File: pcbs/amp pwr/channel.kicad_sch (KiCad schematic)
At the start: 43 parts

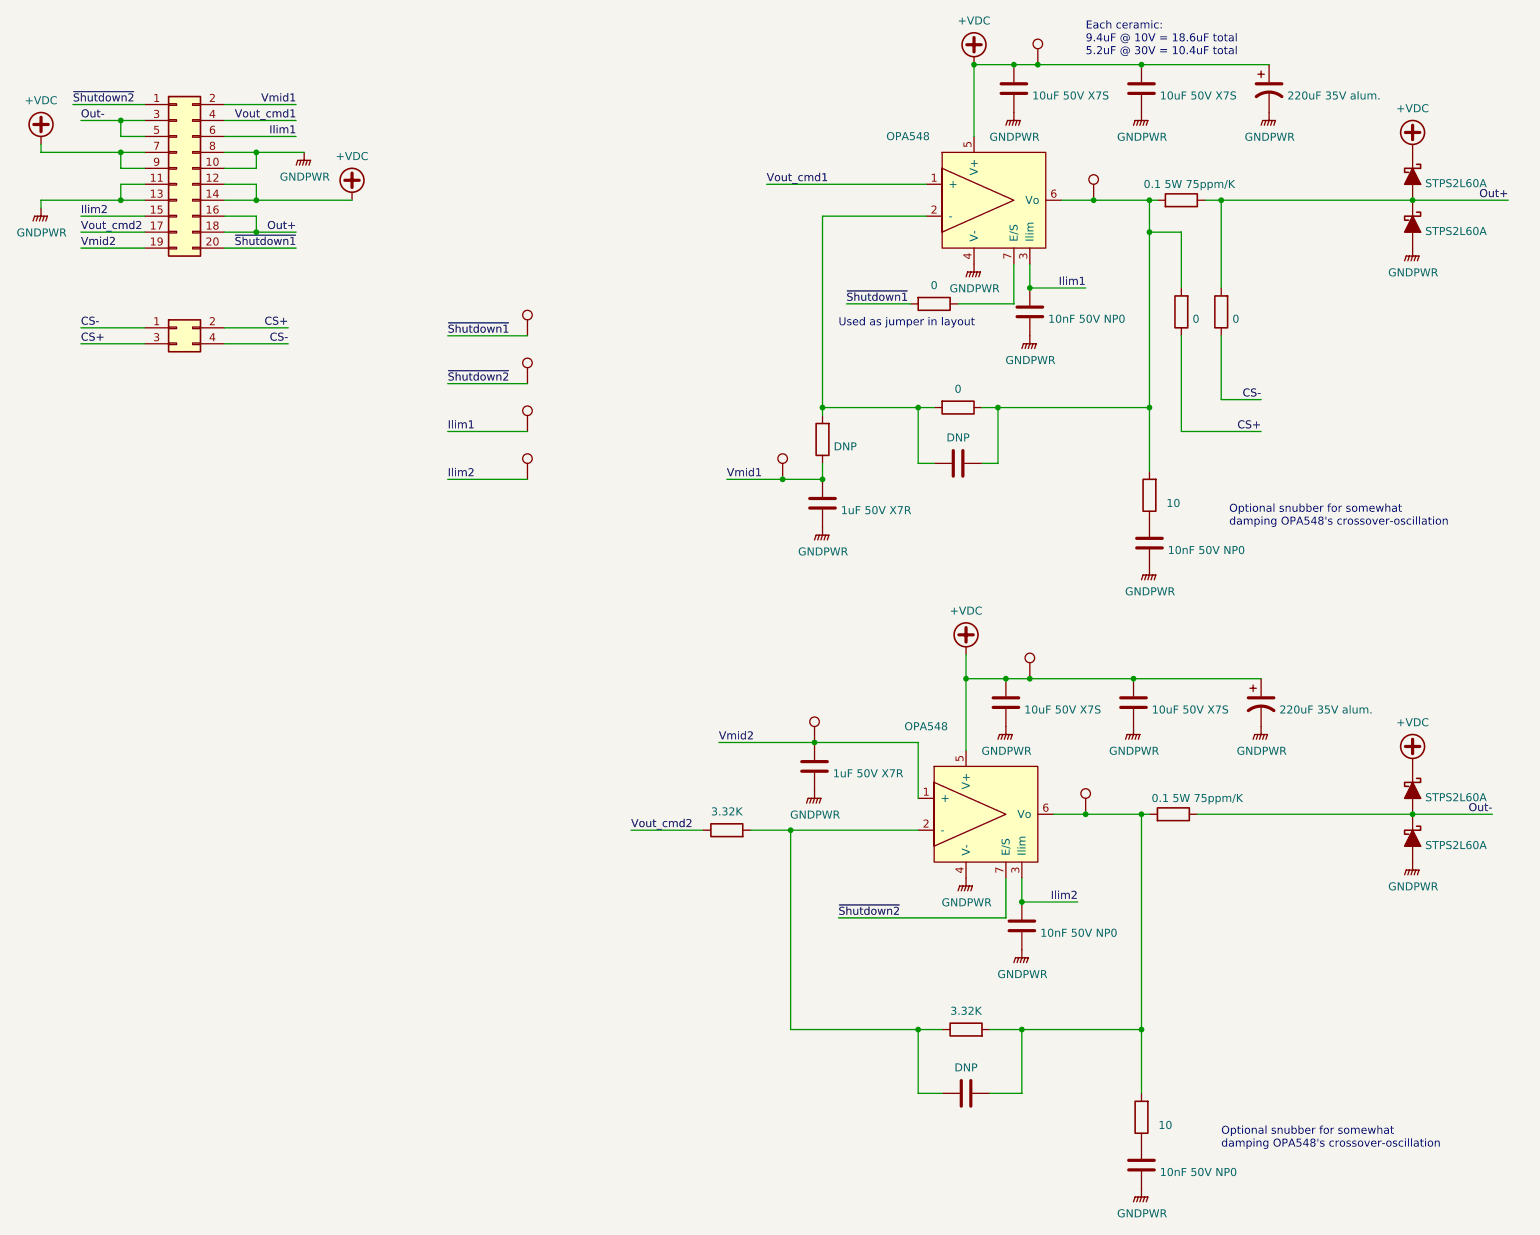
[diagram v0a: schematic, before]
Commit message: Schematic file fix, misc. PCB
Fixed issue with KiCAD's automatic V5→V6 migration (corrected in 6.0.11) that caused problems with component references in multi-channel schematic sheets
Finished migration in amp ctrl PCB, inc. re-assigning "exclude from BOM" attributes to testpoints, solder jumpers
Added mounting hole to amp ctrl PCB for addl support to Ethernet jacks, power connector through stiffener
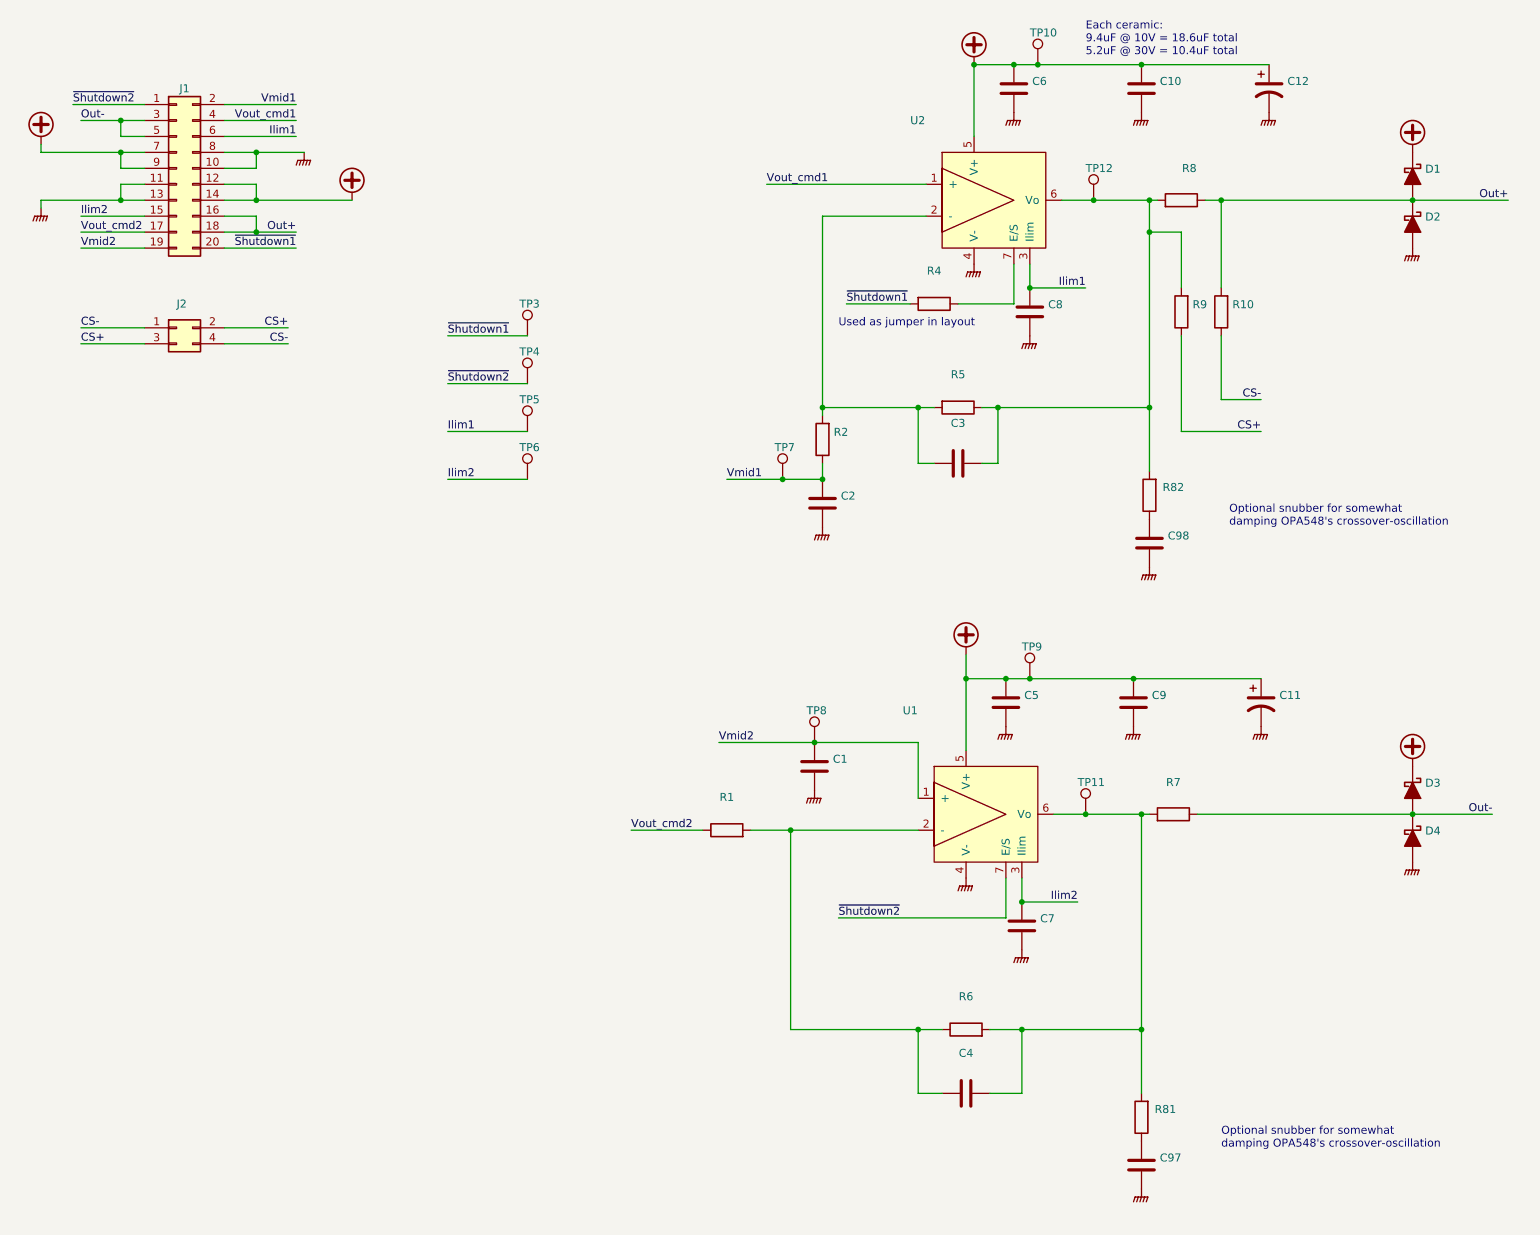
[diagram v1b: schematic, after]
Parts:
- C1, C2: renamed from ?; value 1uF 50V X7R -> (none); footprint Capacitor_SMD:C_1206_3216Metric -> (none)
- C10, C5, C6, C9: renamed from ?; value 10uF 50V X7S -> (none); footprint Capacitor_SMD:C_1210_3225Metric -> (none)
- C11, C12: renamed from ?; value 220uF 35V alum. -> (none); footprint Capacitor_SMD:CP_Elec_8x6.9 -> (none)
- C3, C4: renamed from ?; value DNP -> (none); footprint Capacitor_SMD:C_0805_2012Metric -> (none)
- C7, C8, C97, C98: renamed from ?; value 10nF 50V NP0 -> (none); footprint Capacitor_SMD:C_0603_1608Metric -> (none)
- D1, D2, D3, D4: renamed from ?; value STPS2L60A -> (none); footprint Diode_SMD:D_SMA -> (none)
- J1: renamed from ?; value Conn_02x10_Odd_Even -> (none); footprint Connector_PinHeader_2.54mm:PinHeader_2x10_P2.54mm_Vertical_SMD -> (none)
- J2: renamed from ?; value Conn_02x02_Odd_Even -> (none); footprint Connector_PinHeader_2.54mm:PinHeader_2x02_P2.54mm_Vertical_SMD -> (none)
- R1, R6: renamed from ?; value 3.32K -> (none); footprint Resistor_SMD:R_1206_3216Metric -> (none)
- R10, R9: renamed from ?; value 0 -> (none); footprint Resistor_SMD:R_0603_1608Metric -> (none)
- R2: renamed from ?; value DNP -> (none); footprint Resistor_SMD:R_1206_3216Metric -> (none)
- R4, R5: renamed from ?; value 0 -> (none); footprint Resistor_SMD:R_1206_3216Metric -> (none)
- R7, R8: renamed from ?; value 0.1 5W 75ppm/K -> (none); footprint Martinos:R_Shunt_Vishay_WSR5_KelvinConnection -> (none)
- R81, R82: renamed from ?; value 10 -> (none); footprint Resistor_SMD:R_1206_3216Metric -> (none)
- TP10, TP11, TP12, TP3, TP4, TP5, TP6, TP7, TP8, TP9: renamed from ?; value TestPoint -> (none); footprint TestPoint:TestPoint_Pad_D1.5mm -> (none)
- U1, U2: renamed from ?; value OPA548 -> (none); footprint Package_TO_SOT_SMD:TO-263-7_TabPin4 -> (none)

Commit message: Upgraded to KiCAD 7.0 format Added 10µF cap to ADC's REFP pins to fix the voltage reference output (#15) Corrected ADC & DAC reset by adding a separate reset circuit (#14) Increased Cfbk compensation cap on each channel to work out-of-the-box with small coils (#16)
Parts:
- C1, C2: value (none) -> 1uF 50V X7R; footprint (none) -> Capacitor_SMD:C_1206_3216Metric
- C10, C5, C6, C9: value (none) -> 10uF 50V X7S; footprint (none) -> Capacitor_SMD:C_1210_3225Metric
- C11, C12: value (none) -> 220uF 35V alum.; footprint (none) -> Capacitor_SMD:CP_Elec_8x6.9
- C3, C4: value (none) -> DNP; footprint (none) -> Capacitor_SMD:C_0805_2012Metric
- C7, C8, C97, C98: value (none) -> 10nF 50V NP0; footprint (none) -> Capacitor_SMD:C_0603_1608Metric
- D1, D2, D3, D4: value (none) -> STPS2L60A; footprint (none) -> Diode_SMD:D_SMA
- J1: value (none) -> Conn_02x10_Odd_Even; footprint (none) -> Connector_PinHeader_2.54mm:PinHeader_2x10_P2.54mm_Vertical_SMD
- J2: value (none) -> Conn_02x02_Odd_Even; footprint (none) -> Connector_PinHeader_2.54mm:PinHeader_2x02_P2.54mm_Vertical_SMD
- R1, R6: value (none) -> 3.32K; footprint (none) -> Resistor_SMD:R_1206_3216Metric
- R10, R9: value (none) -> 0; footprint (none) -> Resistor_SMD:R_0603_1608Metric
- R2: value (none) -> DNP; footprint (none) -> Resistor_SMD:R_1206_3216Metric
- R4, R5: value (none) -> 0; footprint (none) -> Resistor_SMD:R_1206_3216Metric
- R7, R8: value (none) -> 0.1 5W 75ppm/K; footprint (none) -> Martinos:R_Shunt_Vishay_WSR5_KelvinConnection
- R81, R82: value (none) -> 10; footprint (none) -> Resistor_SMD:R_1206_3216Metric
- TP10, TP11, TP12, TP3, TP4, TP5, TP6, TP7, TP8, TP9: value (none) -> TestPoint; footprint (none) -> TestPoint:TestPoint_Pad_D1.5mm
- U1, U2: value (none) -> OPA548; footprint (none) -> Package_TO_SOT_SMD:TO-263-7_TabPin4

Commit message: Moved all project-specific symbols & footprints into new "shim" libraries Updated projects to reference the new "shim" library
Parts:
- R7, R8: footprint Martinos:R_Shunt_Vishay_WSR5_KelvinConnection -> shim:R_Shunt_Vishay_WSR5_KelvinConnection
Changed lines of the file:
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@@
 			)
 		)
-		(property "Footprint" "Martinos:R_Shunt_Vishay_WSR5_KelvinConnection"
+		(property "Footprint" "shim:R_Shunt_Vishay_WSR5_KelvinConnection"
 			(at 262.89 80.518 90)
 			(effects
@@
 			)
 		)
-		(property "Footprint" "Martinos:R_Shunt_Vishay_WSR5_KelvinConnection"
+		(property "Footprint" "shim:R_Shunt_Vishay_WSR5_KelvinConnection"
 			(at 261.62 178.308 90)
 			(effects
